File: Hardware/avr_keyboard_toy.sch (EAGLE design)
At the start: 1 part, among them U1 ATMEGA328P-PU

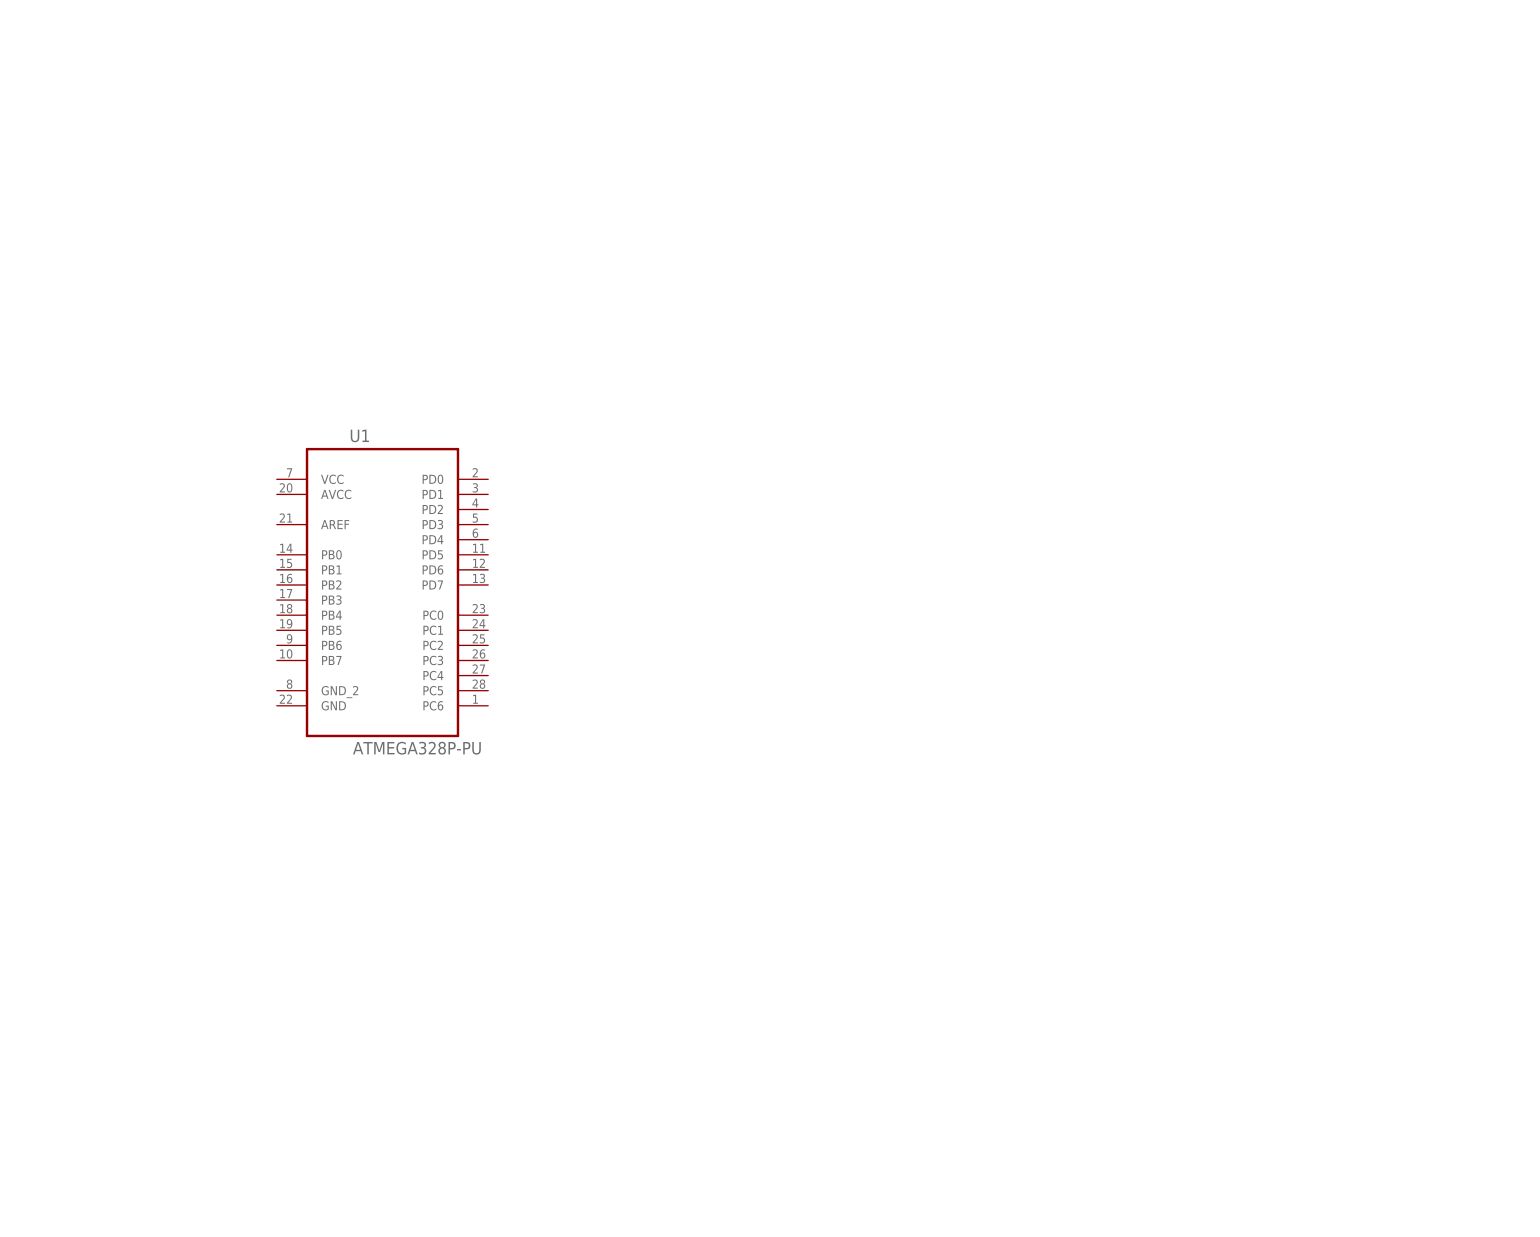
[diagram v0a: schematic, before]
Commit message: All the parts are now on the schematic; now to actually hook them up
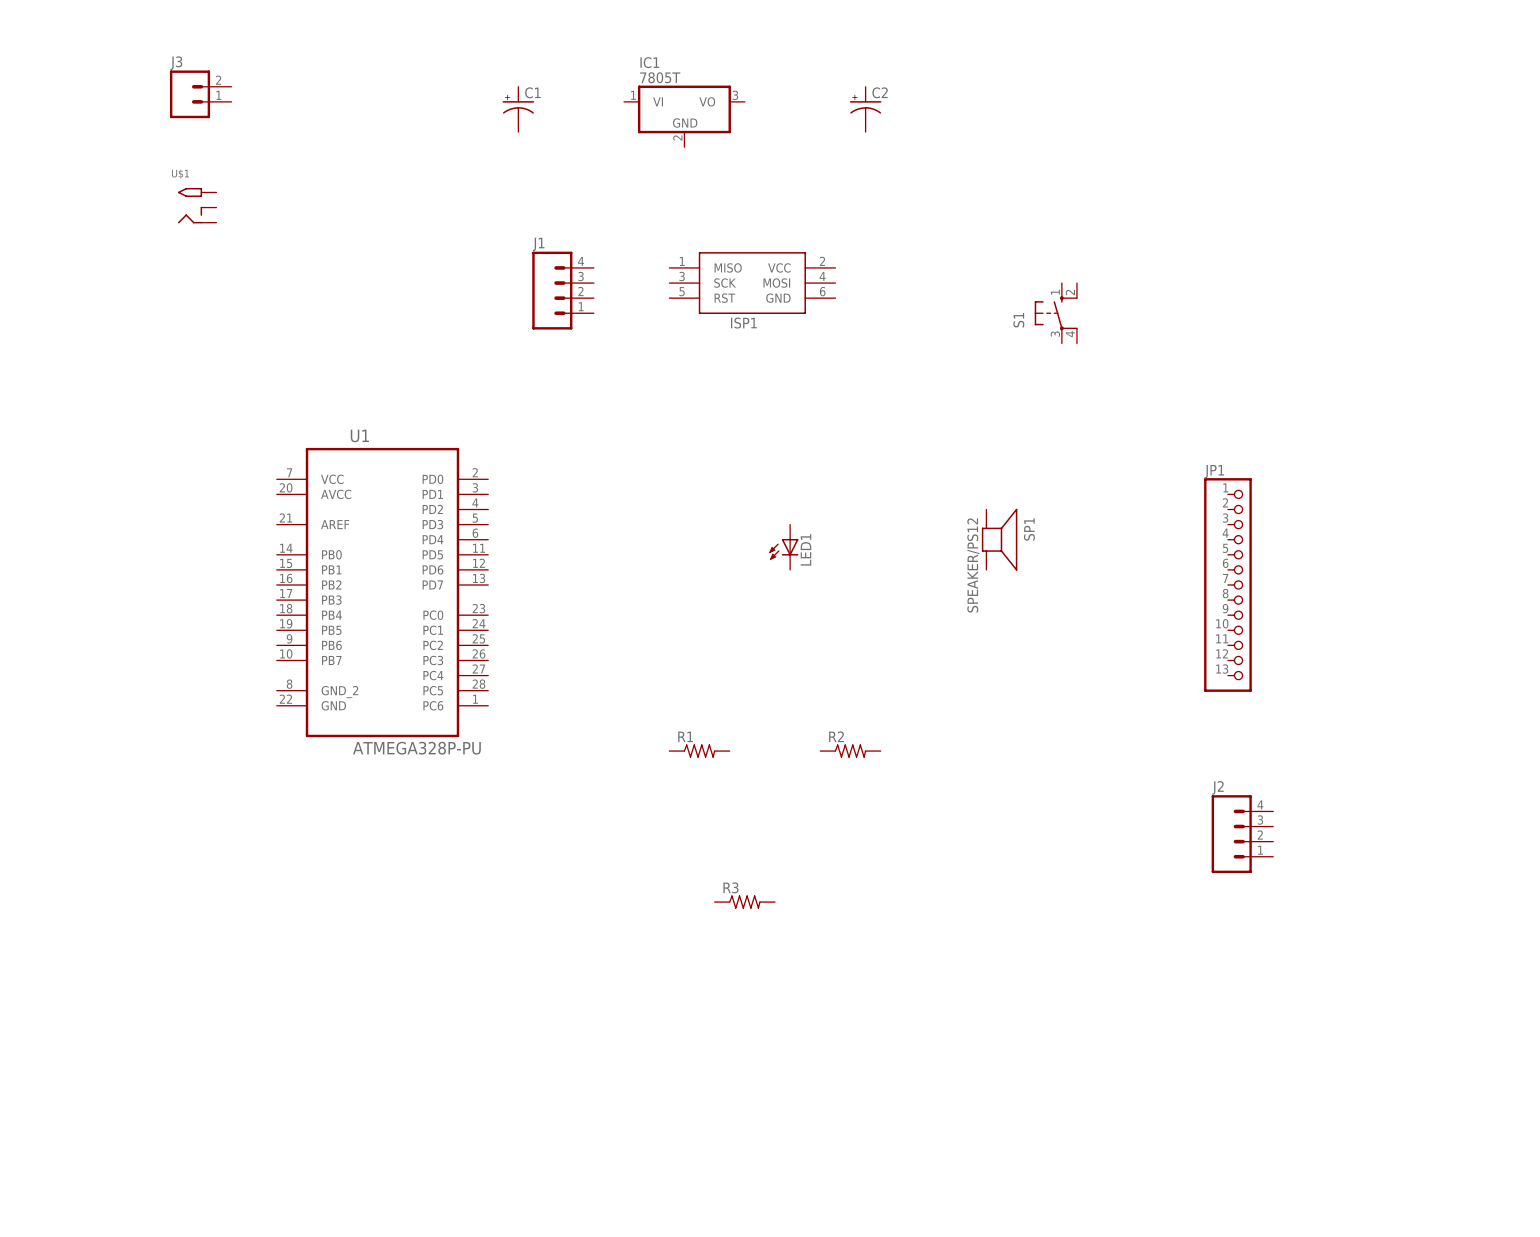
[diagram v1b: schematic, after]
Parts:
- added C1, C2: (no value), adafruit:CPOL-USE1.8-4
- added IC1: 7805T, adafruit:7805T
- added ISP1: AVRISP-6, adafruit:AVRISP-6
- added J1, J2: (no value), SparkFun-Connectors:M04PTH
- added J3: (no value), SparkFun-Connectors:M02PTH
- added JP1: (no value), adafruit:PINHD-1X13
- added LED1: (no value), adafruit:LED3MM
- added R1, R2, R3: (no value), adafruit:R-US_0204/5
- added S1: (no value), switch-omron:10-XX
- added SP1: SPEAKER/PS12, adafruit:SPEAKER/PS12
- added U$1: 2.1MMJACKTHM, adafruit:2.1MMJACKTHM

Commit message: A bunch of work on the schematic; mostly done
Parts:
- removed J2: (no value), SparkFun-Connectors:M04PTH
- removed JP1: (no value), adafruit:PINHD-1X13
- added IC2: MCP23017SP, adafruit:MCP23017SP
- added J5: (no value), SparkFun-Connectors:PINHD-2X10
- added TFT: C-GRID-13-70543, con-molex:C-GRID-13-70543
- added UART: (no value), SparkFun-Connectors:M04PTH
- C1, C2: value (none) -> 10uF
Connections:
- new net +3V3: C2.+, IC1.VO, IC2.!RESET, IC2.VDD, J5.2, J5.4, TFT-12.S, U1.AVCC, U1.VCC
- new net +5V: C1.+, IC1.VI, UART.4
- new net DSP_A0: TFT-10.S, U1.PB0
- new net DSP_RST: TFT-11.S, U1.PB1
- new net GND: C1.-, C2.-, IC1.GND, IC2.A0, IC2.A1, IC2.A2, IC2.VSS, J5.1, J5.3, TFT-13.S, U1.GND, U1.GND_2, UART.3
- new net GPA0: IC2.GPA0, J5.6
- new net GPA1: IC2.GPA1, J5.8
- new net GPA2: IC2.GPA2, J5.10
- new net GPA3: IC2.GPA3, J5.12
- new net GPA4: IC2.GPA4, J5.14
- new net GPA5: IC2.GPA5, J5.16
- new net GPA6: IC2.GPA6, J5.18
- new net GPA7: IC2.GPA7, J5.20
- new net GPB0: IC2.GPB0, J5.5
- new net GPB1: IC2.GPB1, J5.7
- new net GPB2: IC2.GPB2, J5.9
- new net GPB3: IC2.GPB3, J5.11
- new net GPB4: IC2.GPB4, J5.13
- new net GPB5: IC2.GPB5, J5.15
- new net GPB6: IC2.GPB6, J5.17
- new net GPB7: IC2.GPB7, J5.19
- new net LED+: TFT-2.S
- new net LED-: TFT-1.S
- new net MISO: TFT-5.S, U1.PB4
- new net MOSI: TFT-4.S, TFT-9.S, U1.PB3
- new net RST: U1.PC6
- new net RX: U1.PD0, UART.1
- new net SCK: TFT-6.S, TFT-8.S, U1.PB5
- new net SCL: IC2.SCL, U1.PC5
- new net SDA: IC2.SDA, U1.PC4
- new net SD_SS: TFT-3.S, U1.PD7
- new net SS: TFT-7.S, U1.PB2
- new net TX: U1.PD1, UART.2
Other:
- moved on the sheet: C1, C2, IC1

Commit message: Power supplies, mostly
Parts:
- removed J1: (no value), SparkFun-Connectors:M04PTH
- removed J3: (no value), SparkFun-Connectors:M02PTH
- added BAT: (no value), SparkFun-Connectors:M02PTH
- added PS/2: (no value), SparkFun-Connectors:M04PTH
- added S2: (no value), adafruit:EG1218S
- added XTAL1: (no value), SparkFun-FreqCtrl:RESONATORPTH
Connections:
- new net N$1: U1.PB6, XTAL1.1
- new net N$2: U1.PB7, XTAL1.3
- net +3V3: now also BAT.2, U$1.TIP
- net GND: now also BAT.1, U$1.RING, U$1.RING_SW, XTAL1.2
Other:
- moved on the sheet: ISP1, U$1
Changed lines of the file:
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@@
 <part name="SP1" library="adafruit" deviceset="SPEAKER" device="/PS12"/>
 <part name="S1" library="switch-omron" deviceset="10-XX" device=""/>
-<part name="J1" library="SparkFun-Connectors" deviceset="M04" device="PTH"/>
+<part name="PS/2" library="SparkFun-Connectors" deviceset="M04" device="PTH"/>
 <part name="UART" library="SparkFun-Connectors" deviceset="M04" device="PTH"/>
 <part name="U$1" library="adafruit" deviceset="2.1MMJACK" device="THM"/>
-<part name="J3" library="SparkFun-Connectors" deviceset="M02" device="PTH"/>
+<part name="BAT" library="SparkFun-Connectors" deviceset="M02" device="PTH"/>
 <part name="IC1" library="adafruit" deviceset="78*" device="T" technology="05"/>
 <part name="C1" library="adafruit" deviceset="CPOL-US" device="E1.8-4" value="10uF"/>
@@
 <part name="GND6" library="supply1" deviceset="GND" device=""/>
 <part name="P+2" library="supply1" deviceset="+5V" device=""/>
+<part name="S2" library="adafruit" deviceset="EG1218" device="S"/>
+<part name="XTAL1" library="SparkFun-FreqCtrl" deviceset="RESONATOR" device="PTH"/>
+<part name="GND7" library="supply1" deviceset="GND" device=""/>
+<part name="GND8" library="supply1" deviceset="GND" device=""/>
+<part name="GND9" library="supply1" deviceset="GND" device=""/>
+<part name="+3V6" library="supply1" deviceset="+3V3" device=""/>
+<part name="+3V7" library="supply1" deviceset="+3V3" device=""/>
 </parts>
 <sheets>
@@
 <instance part="FRAME1" gate="G$2" x="154.94" y="-10.16"/>
 <instance part="U1" gate="A" x="58.42" y="101.6"/>
-<instance part="ISP1" gate="G$1" x="119.38" y="149.86"/>
+<instance part="ISP1" gate="G$1" x="55.88" y="147.32"/>
 <instance part="LED1" gate="G$1" x="127" y="106.68"/>
 <instance part="R1" gate="G$1" x="111.76" y="71.12"/>
@@
 <instance part="SP1" gate="S1" x="160.02" y="106.68" rot="R270"/>
 <instance part="S1" gate="1" x="172.72" y="144.78"/>
-<instance part="J1" gate="G$1" x="88.9" y="147.32"/>
+<instance part="PS/2" gate="G$1" x="109.22" y="124.46"/>
 <instance part="UART" gate="G$1" x="208.28" y="144.78"/>
-<instance part="U$1" gate="G$1" x="25.4" y="162.56"/>
-<instance part="J3" gate="G$1" x="25.4" y="180.34"/>
+<instance part="U$1" gate="G$1" x="48.26" y="180.34"/>
+<instance part="BAT" gate="G$1" x="88.9" y="177.8"/>
 <instance part="IC1" gate="A1" x="182.88" y="185.42"/>
 <instance part="C1" gate="G$1" x="157.48" y="180.34"/>
@@
 <instance part="GND6" gate="1" x="231.14" y="142.24"/>
 <instance part="P+2" gate="1" x="231.14" y="157.48"/>
+<instance part="S2" gate="1" x="5.08" y="157.48"/>
+<instance part="XTAL1" gate="G$1" x="12.7" y="86.36" rot="R270"/>
+<instance part="GND7" gate="1" x="0" y="71.12"/>
+<instance part="GND8" gate="1" x="66.04" y="172.72"/>
+<instance part="GND9" gate="1" x="109.22" y="172.72"/>
+<instance part="+3V6" gate="G$1" x="109.22" y="187.96"/>
+<instance part="+3V7" gate="G$1" x="66.04" y="187.96"/>
 </instances>
 <busses>
@@
 <wire x1="208.28" y1="185.42" x2="208.28" y2="190.5" width="0.1524" layer="91"/>
 <junction x="208.28" y="185.42"/>
+</segment>
+<segment>
+<pinref part="U$1" gate="G$1" pin="TIP"/>
+<pinref part="+3V7" gate="G$1" pin="+3V3"/>
+<wire x1="53.34" y1="182.88" x2="66.04" y2="182.88" width="0.1524" layer="91"/>
+<wire x1="66.04" y1="182.88" x2="66.04" y2="185.42" width="0.1524" layer="91"/>
+</segment>
+<segment>
+<pinref part="BAT" gate="G$1" pin="2"/>
+<pinref part="+3V6" gate="G$1" pin="+3V3"/>
+<wire x1="96.52" y1="180.34" x2="109.22" y2="180.34" width="0.1524" layer="91"/>
+<wire x1="109.22" y1="180.34" x2="109.22" y2="185.42" width="0.1524" layer="91"/>
 </segment>
 </net>
@@
 <wire x1="231.14" y1="147.32" x2="231.14" y2="144.78" width="0.1524" layer="91"/>
 </segment>
+<segment>
+<pinref part="GND7" gate="1" pin="GND"/>
+<wire x1="0" y1="73.66" x2="0" y2="86.36" width="0.1524" layer="91"/>
+<pinref part="XTAL1" gate="G$1" pin="2"/>
+<wire x1="0" y1="86.36" x2="5.08" y2="86.36" width="0.1524" layer="91"/>
+</segment>
+<segment>
+<pinref part="U$1" gate="G$1" pin="RING"/>
+<pinref part="GND8" gate="1" pin="GND"/>
+<wire x1="53.34" y1="177.8" x2="66.04" y2="177.8" width="0.1524" layer="91"/>
+<wire x1="66.04" y1="177.8" x2="66.04" y2="175.26" width="0.1524" layer="91"/>
+<pinref part="U$1" gate="G$1" pin="RING_SW"/>
+<wire x1="53.34" y1="180.34" x2="66.04" y2="180.34" width="0.1524" layer="91"/>
+<wire x1="66.04" y1="180.34" x2="66.04" y2="177.8" width="0.1524" layer="91"/>
+<junction x="66.04" y="177.8"/>
+</segment>
+<segment>
+<pinref part="BAT" gate="G$1" pin="1"/>
+<pinref part="GND9" gate="1" pin="GND"/>
+<wire x1="96.52" y1="177.8" x2="109.22" y2="177.8" width="0.1524" layer="91"/>
+<wire x1="109.22" y1="177.8" x2="109.22" y2="175.26" width="0.1524" layer="91"/>
+</segment>
 </net>
 <net name="SS" class="0">
@@
 </segment>
 </net>
+<net name="N$1" class="0">
+<segment>
+<pinref part="XTAL1" gate="G$1" pin="1"/>
+<pinref part="U1" gate="A" pin="PB6"/>
+<wire x1="12.7" y1="88.9" x2="40.64" y2="88.9" width="0.1524" layer="91"/>
+</segment>
+</net>
+<net name="N$2" class="0">
+<segment>
+<pinref part="XTAL1" gate="G$1" pin="3"/>
+<wire x1="12.7" y1="83.82" x2="22.86" y2="83.82" width="0.1524" layer="91"/>
+<wire x1="22.86" y1="83.82" x2="22.86" y2="86.36" width="0.1524" layer="91"/>
+<pinref part="U1" gate="A" pin="PB7"/>
+<wire x1="22.86" y1="86.36" x2="40.64" y2="86.36" width="0.1524" layer="91"/>
+</segment>
+</net>

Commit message: Mostly finished
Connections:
- removed net LED+: TFT-2.S
- removed net LED-: TFT-1.S
- new net N$3: LED1.A, R1.2
- new net N$4: R2.2, SP1.+
- new net PIEZO: R2.1, U1.PD5
- new net PS/2_CLK: U1.PD3
- new net PS/2_CLOCK: PS/2.2
- new net PS/2_DATA: PS/2.3, U1.PD4
- new net VCC: IC2.!RESET, IC2.VDD, ISP1.VCC, J5.2, J5.4, PS/2.4, R3.1, S2.S, TFT-12.S, TFT-2.S, U1.AVCC, U1.VCC
- net +3V3: now also S2.P; no longer IC2.!RESET, IC2.VDD, J5.2, J5.4, TFT-12.S, U1.AVCC, U1.VCC
- net GND: now also ISP1.GND, LED1.C, PS/2.1, S1.S, S1.S1, SP1.-, TFT-1.S
- net MISO: now also ISP1.MISO
- net MOSI: now also ISP1.MOSI
- net RST: now also ISP1.RST, R3.2, S1.P, S1.P1
- net SCK: now also ISP1.SCK, R1.1
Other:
- moved on the sheet: LED1, PS/2, R1, R2, R3, S1, S2, SP1
